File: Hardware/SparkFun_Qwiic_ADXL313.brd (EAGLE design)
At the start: 25.4 x 25.4 mm, 58 parts, among them J2 QWIIC_RA, J4 QWIIC_RA, U1 ADXL313

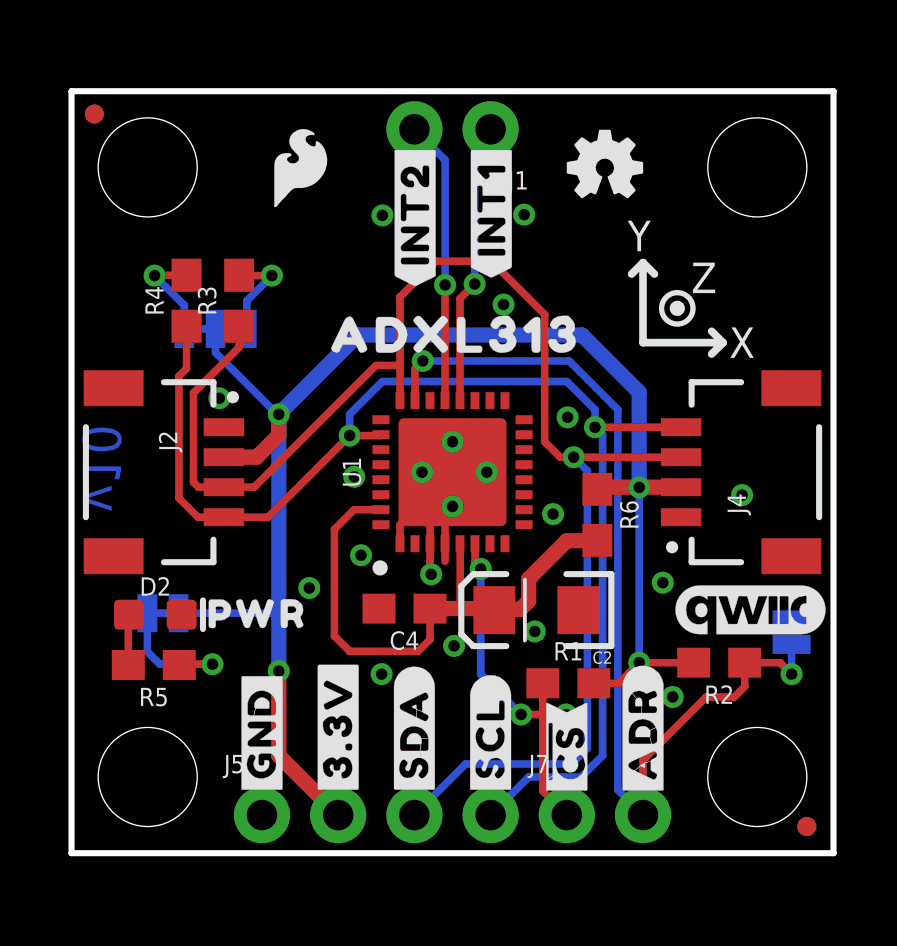
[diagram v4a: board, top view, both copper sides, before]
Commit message: More changes from review #2
-INPUTS and OUTPUT silk flags corrected
-XYZ axis silk rotated 90 degress to match IC axis. on both top and bottom silk.
-Removed label on top silk for CS pin (because it's not part of I2C).
-Swapped CD and ADR/SDO, so that all I2C pins are in a a row.
-Changed ADR silk label on top so that it is an INPUT flag silk type
-rotated I2C jumper (and silk) so that all bottom silk reads the same direction.
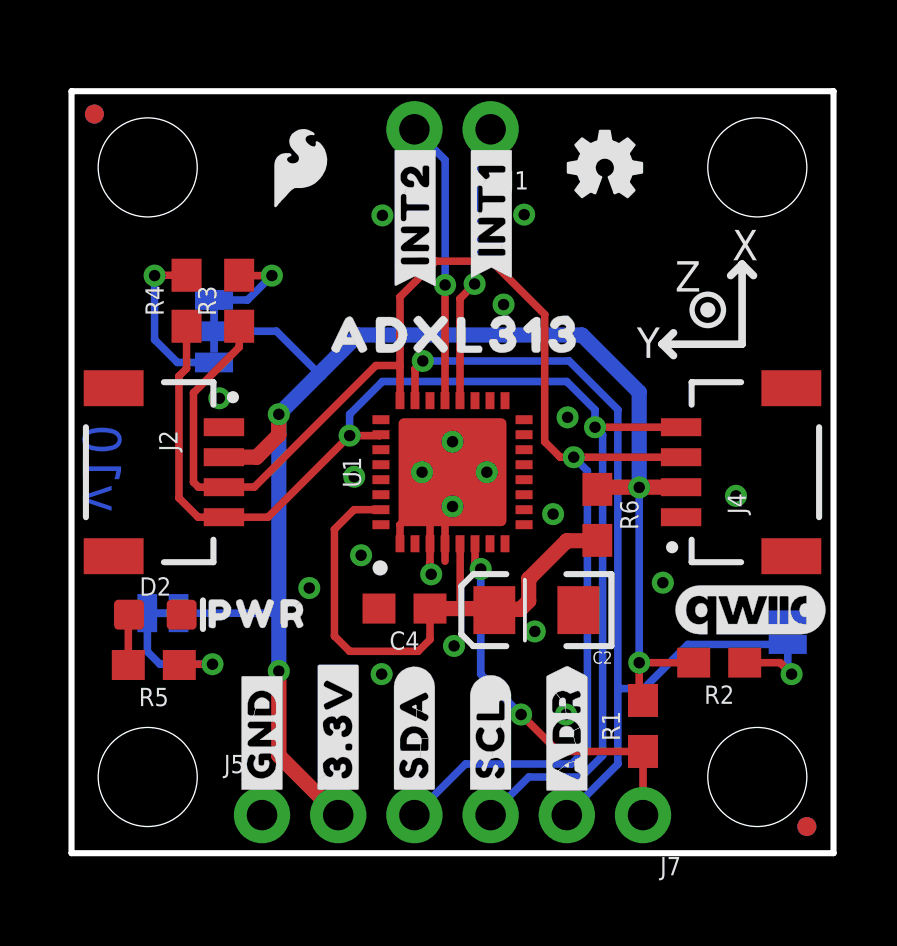
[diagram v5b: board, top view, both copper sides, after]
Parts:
- removed U$17: (no value), output:##CS##0
- removed U$21: (no value), output:#ADR#0
- added U$12: (no value), output:#_ADR#0
- moved U$27 3.46 mm to (3.12, 19.3), turned to 90 degrees
- moved R1 2.87 mm to (19.1, 4.24), turned to 90 degrees
- moved J7 2.54 mm to (19.1, 1.27), turned to 180 degrees
- moved U$18 2.54 mm to (19.1, 1.75)
- moved U$28 2.54 mm to (16.5, 1.75)
- moved U$30 2.54 mm to (16.5, 1.75)
- moved U$23 0.25 mm to (21.1, 9.27)
- moved U$22 0.18 mm to (22.2, 9.22)
- moved ADR 0.13 mm to (23.9, 7.37)
- moved I2C 0.09 mm to (4.75, 17.4), turned to 270 degrees
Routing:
- net N$2: track 3.26 -> 5.50 mm
- net !CS: track 11.8 -> 13.0 mm
- net GND: vias 21 -> 20
